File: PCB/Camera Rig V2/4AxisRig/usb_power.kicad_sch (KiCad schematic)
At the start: 27 parts, among them U1 TPS25730DREFR

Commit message: PCB V2 first draft
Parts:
- added TP1: TestPoint, TestPoint:TestPoint_Pad_2.0x2.0mm, symbol Connector:TestPoint
- C1, C10, C11, C12, C13, C2, C3, C4, C5, C6, C9: footprint (none) -> Capacitor_SMD:C_0603_1608Metric_Pad1.08x0.95mm_HandSolder
- C7, C8: footprint (none) -> Capacitor_SMD:C_1206_3216Metric_Pad1.33x1.80mm_HandSolder
- U1: Unique FP y -> (none)
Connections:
- net CAP_MIS: now also TP1.1
- net CC1 renamed USB_CC1
- net CC2 renamed USB_CC2
- no-connect marks 9 -> 8
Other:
- sheet USB Connector ports: added USB_CC1, USB_CC2; removed CC1, CC2

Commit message: Updated figs
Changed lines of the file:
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@@
 	(wire
 		(pts
-			(xy 104.14 78.74) (xy 114.3 78.74)
+			(xy 107.95 78.74) (xy 114.3 78.74)
 		)
 		(stroke
@@
 	(hierarchical_label "PPHV"
 		(shape output)
-		(at 104.14 78.74 180)
-		(effects
-			(font
+		(at 107.95 78.74 180)
+		(effects
+			(font

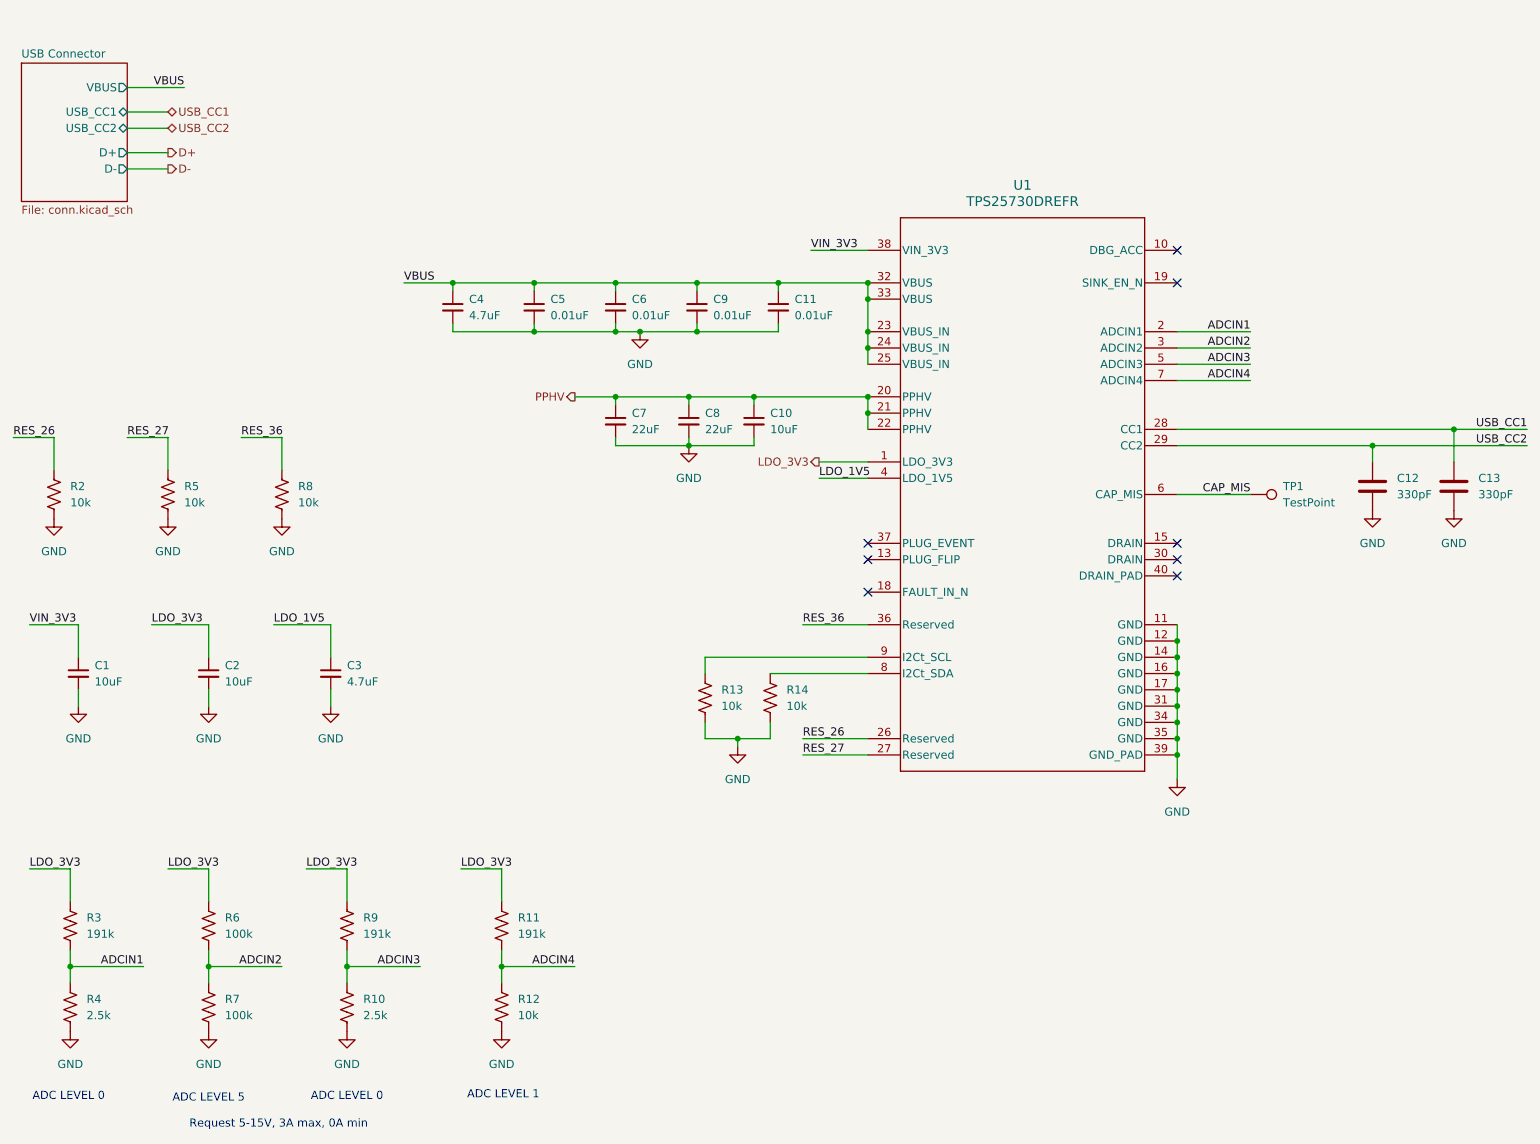
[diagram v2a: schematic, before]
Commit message: Netclass Improvements
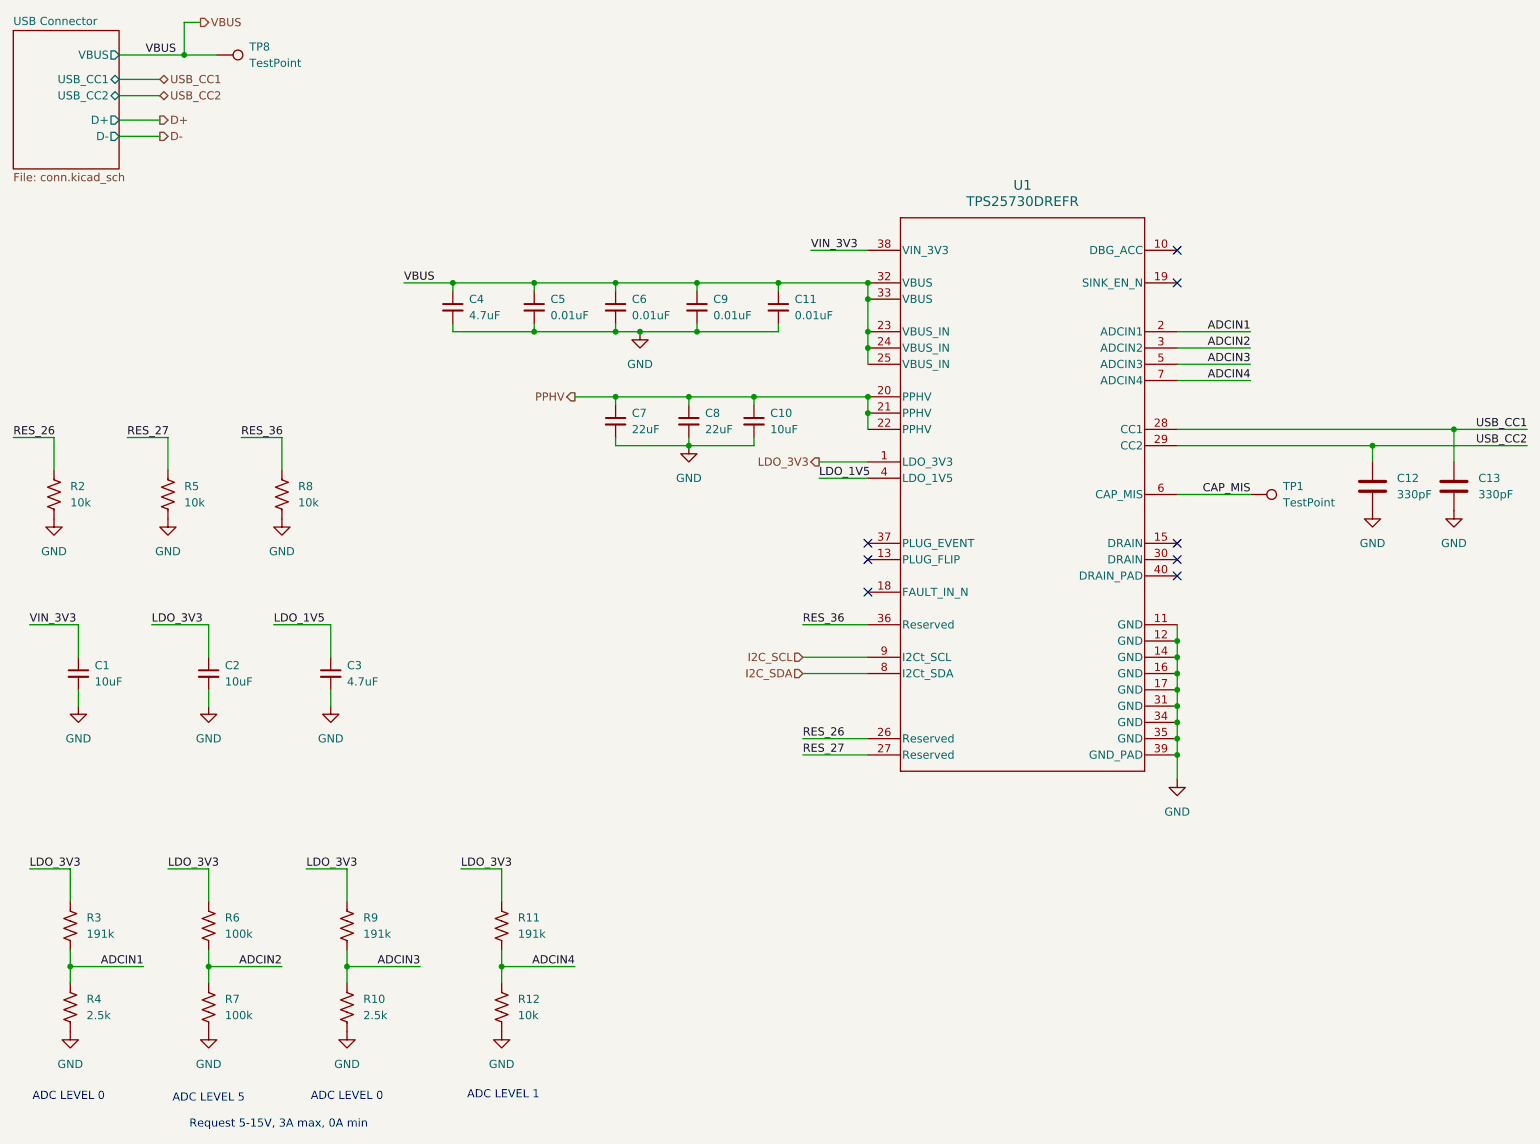
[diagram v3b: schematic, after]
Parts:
- removed R13, R14: 10k, Resistor_SMD:R_0603_1608Metric_Pad0.98x0.95mm_HandSolder, symbol Device:R_US
- added TP8: TestPoint, TestPoint:TestPoint_Pad_1.0x1.0mm, symbol Connector:TestPoint
- TP1: footprint TestPoint:TestPoint_Pad_2.0x2.0mm -> TestPoint:TestPoint_Pad_1.0x1.0mm
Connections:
- net VBUS: now also TP8.1
- net I2C_SDA: now reaches U1.8 (I2Ct_SDA)
- net I2C_SCL: now reaches U1.9 (I2Ct_SCL)
